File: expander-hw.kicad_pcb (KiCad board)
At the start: 2 copper layers, 44.2 x 22.6 mm, 29 parts, among them J1 Conn_ARM_SWD_TagConnect_TC203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, J2 USB_C_Receptacle_USB2.0_16P, J3 Conn_02x08_Odd_Even, U1 STM32H523RETx, U2 USBLC6-2SC6, U3 AZ1117-3.3, U4 SRDA3.3-4BTG, U5 SRDA3.3-4BTG, U6 SRDA3.3-4BTG

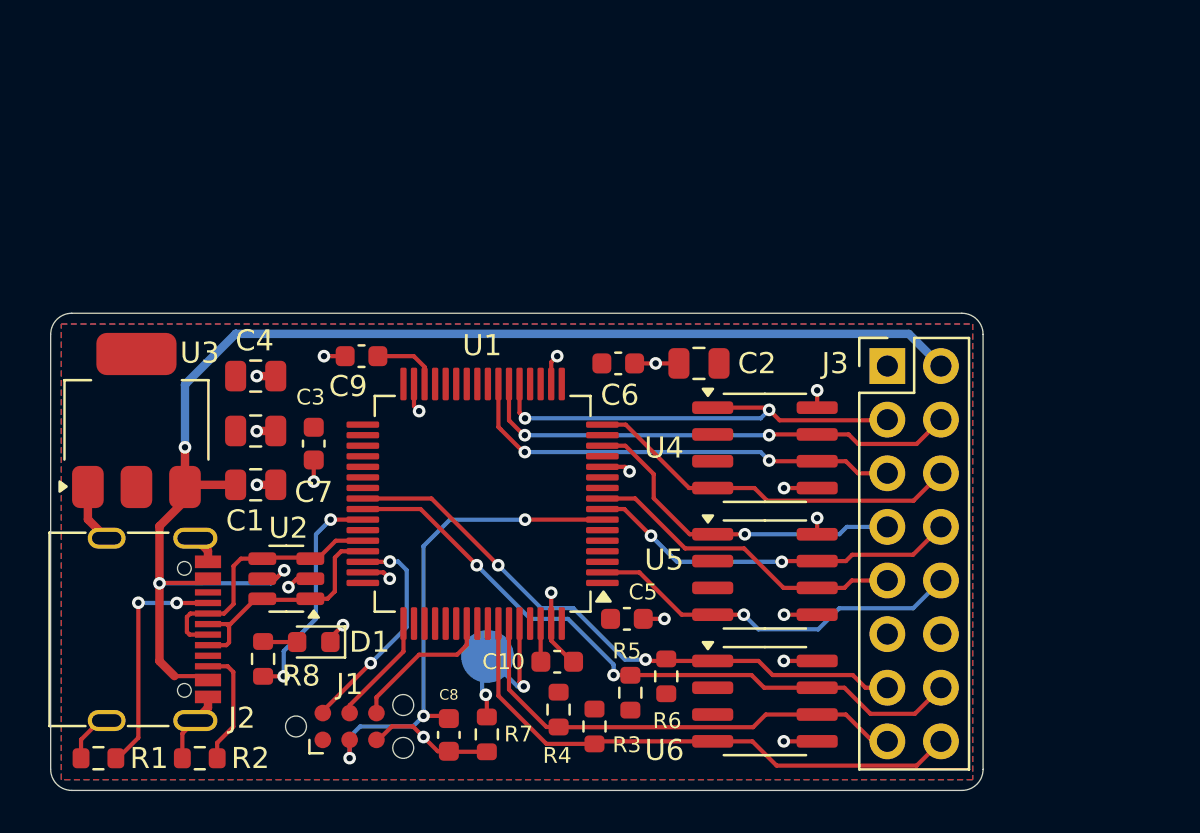
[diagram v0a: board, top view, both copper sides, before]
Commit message: Add DAC hardware
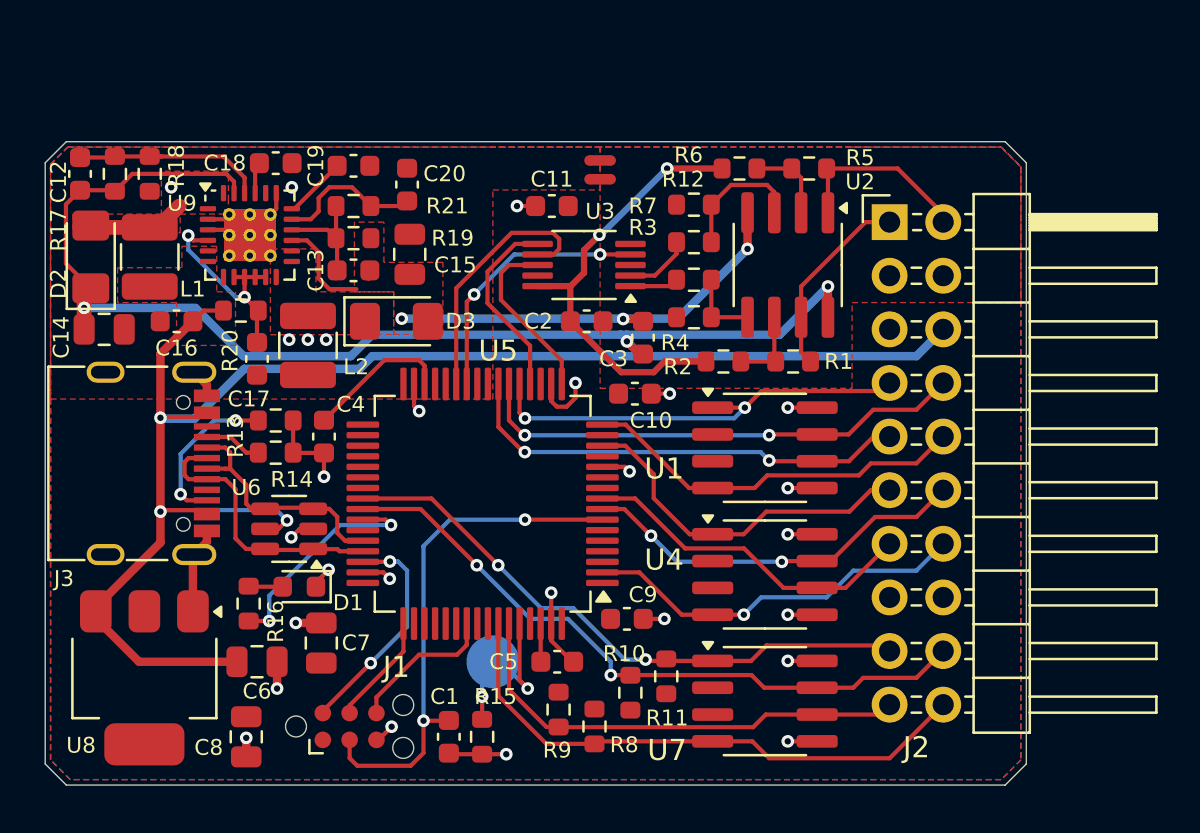
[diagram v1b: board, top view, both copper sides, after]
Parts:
- removed BOOT: TestPoint_Pad_D2.5mm, TestPoint:TestPoint_Pad_D2.5mm
- removed the J3 at (148.0, 92.9)
- added C12: 6.8pF, Capacitor_SMD:C_0603_1608Metric, F.Cu at (109.7, 83.8)
- added C13: 7.5pF, Capacitor_SMD:C_0603_1608Metric, F.Cu at (122.7, 88.4)
- added C14: 22uF, Capacitor_SMD:C_0805_2012Metric, F.Cu at (110.9, 91.2)
- added C15: 22uF, Capacitor_SMD:C_0805_2012Metric, F.Cu at (125.3, 87.6)
- added C16: 10uF, Capacitor_SMD:C_0603_1608Metric, F.Cu at (114.3, 90.8)
- added C17: 100nF, Capacitor_SMD:C_0603_1608Metric, F.Cu at (118.1, 92.6)
- added C18: 10nF, Capacitor_SMD:C_0603_1608Metric, F.Cu at (119.0, 83.3)
- added C19: 4.7nF, Capacitor_SMD:C_0603_1608Metric, F.Cu at (122.7, 83.4)
- added C20: 220nF, Capacitor_SMD:C_0603_1608Metric, F.Cu at (125.2, 84.3)
- added C3: 100nF, Capacitor_SMD:C_0603_1608Metric, F.Cu at (136.4, 91.6)
- added D2: D_Schottky, Diode_SMD:D_1206_3216Metric_Pad1.42x1.75mm_HandSolder, F.Cu at (110.2, 87.8)
- added D3: D_Schottky, Diode_SMD:D_1206_3216Metric_Pad1.42x1.75mm_HandSolder, F.Cu at (124.7, 90.8)
- added J2: Conn_02x10_Odd_Even, Connector_PinHeader_2.54mm:PinHeader_2x10_P2.54mm_Horizontal, F.Cu at (148.1, 86.1)
- added L1: 4.7uH, Inductor_SMD:L_1210_3225Metric, F.Cu at (113.0, 87.8)
- added L2: 4.7uH, Inductor_SMD:L_1210_3225Metric, F.Cu at (120.5, 91.9)
- added NT1: NetTie_2, NetTie:NetTie-2_SMD_Pad0.5mm, F.Cu at (134.4, 83.2)
- added NT2: NetTie_2, NetTie:NetTie-2_SMD_Pad0.5mm, F.Cu at (134.4, 84.1)
- added R1: 100k, Resistor_SMD:R_0603_1608Metric, F.Cu at (143.5, 92.7)
- added R12: 100k, Resistor_SMD:R_0603_1608Metric, F.Cu at (138.8, 85.3)
- added R17: 900k, Resistor_SMD:R_0603_1608Metric, F.Cu at (111.4, 83.8)
- added R18: 100k, Resistor_SMD:R_0603_1608Metric, F.Cu at (113.0, 83.8)
- added R19: 1M, Resistor_SMD:R_0603_1608Metric, F.Cu at (122.7, 86.9)
- added R2: 10k, Resistor_SMD:R_0603_1608Metric, F.Cu at (140.2, 92.7)
- added R20: 100, Resistor_SMD:R_0603_1608Metric, F.Cu at (117.3, 90.3)
- added R21: 100k, Resistor_SMD:R_0603_1608Metric, F.Cu at (122.7, 85.3)
- added R3: 10k, Resistor_SMD:R_0603_1608Metric, F.Cu at (138.8, 88.8)
- added R4: 100k, Resistor_SMD:R_0603_1608Metric, F.Cu at (138.8, 90.6)
- added R5: 100k, Resistor_SMD:R_0603_1608Metric, F.Cu at (144.3, 83.6)
- added R6: 10k, Resistor_SMD:R_0603_1608Metric, F.Cu at (141.0, 83.6)
- added R7: 10k, Resistor_SMD:R_0603_1608Metric, F.Cu at (138.8, 87.1)
- added TP1: BOOT, TestPoint:TestPoint_Pad_D2.5mm, B.Cu at (129.3, 106.9)
- added U2: OPA2994xD, Package_SO:SOIC-8_3.9x4.9mm_P1.27mm, F.Cu at (143.3, 88.1)
- added U3: DAC8562, Package_SO:VSSOP-10_3x3mm_P0.5mm, F.Cu at (133.6, 88.1)
- added U9: TPS65130RGE, Package_DFN_QFN:VQFN-24-1EP_4x4mm_P0.5mm_EP2.45x2.45mm_ThermalVias, F.Cu at (117.8, 86.7)
- C2: value 10uF -> 150nF; footprint Capacitor_SMD:C_0805_2012Metric -> Capacitor_SMD:C_0603_1608Metric
- moved C8 17.1 mm to (117.6, 110.5), turned to -90 degrees
- moved R14 16.7 mm to (119.0, 97.0), turned to 0 degrees
- moved R13 16.4 mm to (119.0, 95.5), turned to 0 degrees
- moved C11 15.9 mm to (132.1, 85.3), turned to 180 degrees
- moved U8 12.2 mm to (112.8, 107.7), turned to -90 degrees
- moved C7 10.5 mm to (121.2, 106.0), turned to 90 degrees
- moved C6 8.38 mm to (118.1, 106.9)
- moved J3 7.86 mm to (112.0, 97.5)
- moved C2 5.68 mm to (133.7, 90.8), turned to 0 degrees
- moved C4 4.20 mm to (121.3, 96.3), turned to -90 degrees
- moved R16 2.71 mm to (117.7, 104.2)
- moved D1 2.71 mm to (120.1, 103.4)
- moved U6 2.37 mm to (119.6, 100.6)
- moved C10 1.64 mm to (136.0, 94.2)
- moved R15 0.25 mm to (128.8, 110.5)
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- renumbered C8 to C1, C6 to C10, C7 to C11, C9 to C4, C10 to C5, C1 to C6, C3 to C7, C4 to C8, C5 to C9, J2 to J3, R5 to R10, R6 to R11, R2 to R13, R1 to R14, R7 to R15, R8 to R16, R3 to R8, R4 to R9, U4 to U1, U5 to U4, U1 to U5, U2 to U6, U6 to U7, U3 to U8
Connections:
- C2 pad 1: +3.3V -> Net-(U3-V_{REF}IN/OUT)
- C2 pad 2: GND -> GNDA
- U5 pad 17: unconnected-(U1-PA3-Pad17) -> /DAC_DIN
- U5 pad 20: unconnected-(U1-PA4-Pad20) -> /DAC_SYNC
- U5 pad 26: unconnected-(U1-PB0-Pad26) -> /DAC_LOAD
- U5 pad 27: unconnected-(U1-PB1-Pad27) -> /DAC_CLK
- U5 pad 33: /HW_V0 -> +3.3V
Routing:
- net +12V: track 0.00 -> 56.5 mm, vias 0 -> 3
- net -12V: track 0.00 -> 25.5 mm, vias 0 -> 3
- net Net-(U3-V_{REF}IN/OUT): track 0.00 -> 20.8 mm, vias 0 -> 2
- net /DAC_LOAD: track 0.00 -> 12.6 mm, vias 0 -> 2
- net /DAC_CLK: track 0.00 -> 12.2 mm
- net Net-(U9-ENN): track 0.00 -> 10.5 mm, vias 0 -> 2
- net VBUS: track 65.9 -> 75.5 mm
- net /A0: track 0.00 -> 9.19 mm
- net /DAC_SYNC: track 0.00 -> 9.08 mm
- net /A1: track 0.00 -> 8.92 mm
- net Net-(U9-FBP): track 0.00 -> 8.67 mm
- net /DAC_DIN: track 0.00 -> 8.34 mm
- net Net-(J3-CC1): track 11.2 -> 2.87 mm, vias 2 -> 0
- net Net-(U9-VREF): track 0.00 -> 6.96 mm
- net Net-(U2A-+): track 0.00 -> 6.27 mm
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- added copper zone on F.Cu, net -12V
- added copper zone on F.Cu, net CoilNeg
- added copper zone on F.Cu, net CoilPos
- added copper zone on F.Cu, net GND
- added copper zone on F.Cu, net GNDA
- added copper zone on F.Cu, net VBUS
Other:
- board size 44.2 x 22.6 mm -> 46.5 x 30.5 mm
- board text added: "HW-V1"
- board text removed: "HW-V0"

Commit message: Fix boost converter + vref
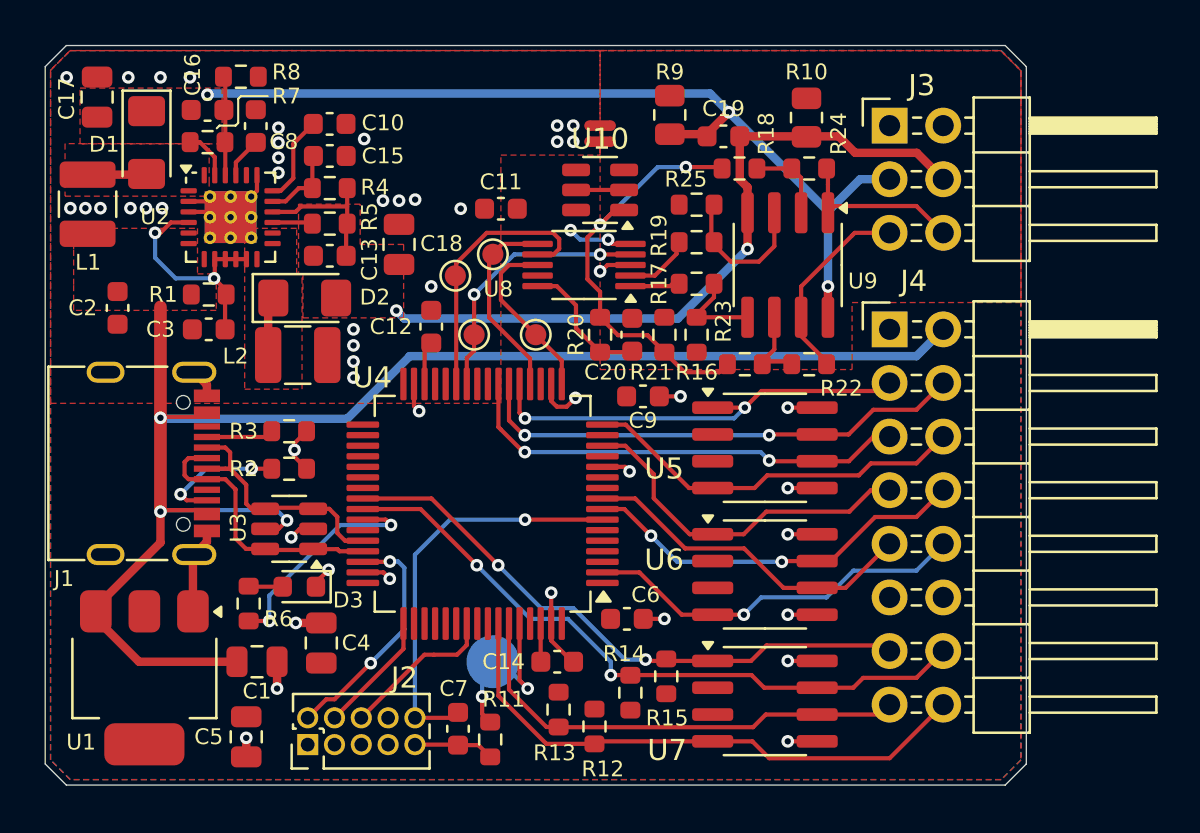
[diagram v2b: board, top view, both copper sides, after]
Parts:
- removed the J1 at (122.5, 110.0)
- added J3: Conn_02x03_Odd_Even, Connector_PinHeader_2.54mm:PinHeader_2x03_P2.54mm_Horizontal, F.Cu at (148.1, 81.5)
- added J4: Conn_02x08_Odd_Even, Connector_PinHeader_2.54mm:PinHeader_2x08_P2.54mm_Horizontal, F.Cu at (148.1, 91.2)
- added R10: 2k, Resistor_SMD:R_0805_2012Metric, F.Cu at (144.1, 81.2)
- added R20: 180, Resistor_SMD:R_0603_1608Metric, F.Cu at (134.4, 91.4)
- added R21: 180, Resistor_SMD:R_0603_1608Metric, F.Cu at (137.4, 91.4)
- added R9: 2k, Resistor_SMD:R_0805_2012Metric, F.Cu at (137.7, 81.0)
- added TP2: CLK, TestPoint:TestPoint_Pad_D1.0mm, F.Cu at (127.5, 88.6)
- added TP3: DIN, TestPoint:TestPoint_Pad_D1.0mm, F.Cu at (131.3, 91.4)
- added TP4: SYNC, TestPoint:TestPoint_Pad_D1.0mm, F.Cu at (129.3, 87.6)
- added TP5: LOAD, TestPoint:TestPoint_Pad_D1.0mm, F.Cu at (128.4, 91.4)
- added U10: MCP1501-10xCH, Package_TO_SOT_SMD:SOT-23-6, F.Cu at (134.4, 84.6)
- C20: renamed from C2; value 150nF -> 10nF
- J2: value Conn_02x10_Odd_Even -> Conn_ARM_JTAG_SWD_10; footprint Connector_PinHeader_2.54mm:PinHeader_2x10_P2.54mm_Horizontal -> Connector_PinHeader_1.27mm:PinHeader_2x05_P1.27mm_Vertical
- moved J2 37.1 mm to (120.5, 110.9), turned to 90 degrees
- moved C17 11.0 mm to (110.5, 80.2), turned to 90 degrees
- moved C19 10.3 mm to (140.2, 82.0), turned to 0 degrees
- moved C12 7.27 mm to (126.4, 91.1), turned to 90 degrees
- moved C16 6.76 mm to (115.8, 80.8), turned to 0 degrees
- moved R8 6.31 mm to (117.3, 79.2), turned to 180 degrees
- moved D1 6.03 mm to (112.9, 82.3), turned to -90 degrees
- moved R7 4.64 mm to (115.8, 82.3), turned to 180 degrees
- moved D2 4.48 mm to (120.4, 89.7)
- moved C15 3.91 mm to (121.6, 83.0), turned to 0 degrees
- moved L1 3.86 mm to (110.1, 85.3)
- moved C2 2.87 mm to (111.5, 90.2), turned to -90 degrees
- moved C3 2.68 mm to (115.8, 91.2), turned to 180 degrees
- moved C11 2.42 mm to (129.7, 85.5)
- moved R2 2.37 mm to (119.6, 97.8)
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- renumbered C6 to C1, C19 to C10, C4 to C12, C5 to C14, C20 to C15, C12 to C16, C14 to C17, C15 to C18, C3 to C19, C16 to C2, C17 to C3, C7 to C4, C8 to C5, C9 to C6, C1 to C7, C18 to C8, C10 to C9, D2 to D1, D3 to D2, D1 to D3, J3 to J1, R20 to R1, R15 to R11, R8 to R12, R9 to R13, R10 to R14, R11 to R15, R2 to R16, R3 to R17, R6 to R18, R7 to R19, R13 to R2, R1 to R22, R4 to R23, R5 to R24, R12 to R25, R14 to R3, R21 to R4, R19 to R5, R16 to R6, R17 to R7, R18 to R8, U8 to U1, U9 to U2, U6 to U3, U5 to U4, U1 to U5, U4 to U6, U3 to U8, U2 to U9
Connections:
- C13 pad 1: -12V -> Net-(U2-FBN)
- C13 pad 2: Net-(U9-FBN) -> -12V
- C15 pad 1: Net-(U9-VREF) -> Net-(U2-VREF)
- C20 pad 1: Net-(U3-V_{REF}IN/OUT) -> Net-(U8-V_{REF}IN/OUT)
- J2 pad 1: /A0 -> +3.3V
- J2 pad 10: /SPI1_CS -> /~{RESET}
- J2 pad 2: /A1 -> /SWDIO
- J2 pad 3: GNDA -> GND
- J2 pad 4: GNDA -> /SWDCLK
- J2 pad 5: +3.3V -> GND
- J2 pad 6: VBUS -> /SWO
- J2 pad 7: /SPI1_SCK -> unconnected-(J2-KEY-Pad7)
- J2 pad 8: /SPI1_MISO -> unconnected-(J2-NC/TDI-Pad8)
- J2 pad 9: /SPI1_MOSI -> GND
- R16 pad 2: Net-(U3-V_{REF}IN/OUT) -> Net-(U10-OUT)
- R18 pad 2: Net-(U3-V_{REF}IN/OUT) -> Net-(U10-OUT)
- R4 pad 1: Net-(U9-VREF) -> Net-(U2-FBN)
- R4 pad 2: Net-(U9-FBN) -> Net-(U2-VREF)
- R5 pad 1: Net-(U9-FBN) -> -12V
- R5 pad 2: -12V -> Net-(U2-FBN)
- U2 pad 16: Net-(U9-FBN) -> Net-(U2-FBN)
- U2 pad 17: Net-(U9-VREF) -> Net-(U2-VREF)
- U8 pad 10: Net-(U3-V_{REF}IN/OUT) -> Net-(U8-V_{REF}IN/OUT)
- U8 pad 3: GNDA -> GND
- U8 pad 5: /DAC_CLR -> +3.3V
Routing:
- net Net-(U3-V_{REF}IN/OUT): track 20.8 -> 0.00 mm, vias 2 -> 0
- net Net-(U10-OUT): track 0.00 -> 20.6 mm, vias 0 -> 2
- net -12V: track 25.5 -> 36.1 mm, vias 3 -> 2
- net +12V: track 56.5 -> 46.0 mm
- net Net-(U2-FBN): track 0.00 -> 6.99 mm
- net Net-(U9-VREF): track 6.96 -> 0.00 mm
- net Net-(U8-V_{REF}IN/OUT): track 0.00 -> 6.43 mm
- net /~{RESET}: track 24.9 -> 19.4 mm, vias 2 -> 1
- net Net-(U9-FBN): track 5.06 -> 0.00 mm
- net Net-(C12-Pad1): track 6.92 -> 2.07 mm
- net Net-(U2-FBP): track 8.67 -> 4.75 mm
- net Net-(U2-VREF): track 0.00 -> 3.72 mm
- net +3.3V: track 0.00 -> 3.10 mm, vias 0 -> 2
- net CoilNeg: track 0.00 -> 2.80 mm
- net GNDA: track 0.00 -> 2.28 mm
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- added copper zone on F.Cu, net +12V
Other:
- board size 46.5 x 30.5 mm -> 46.5 x 35 mm

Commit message: Refactor dac gain
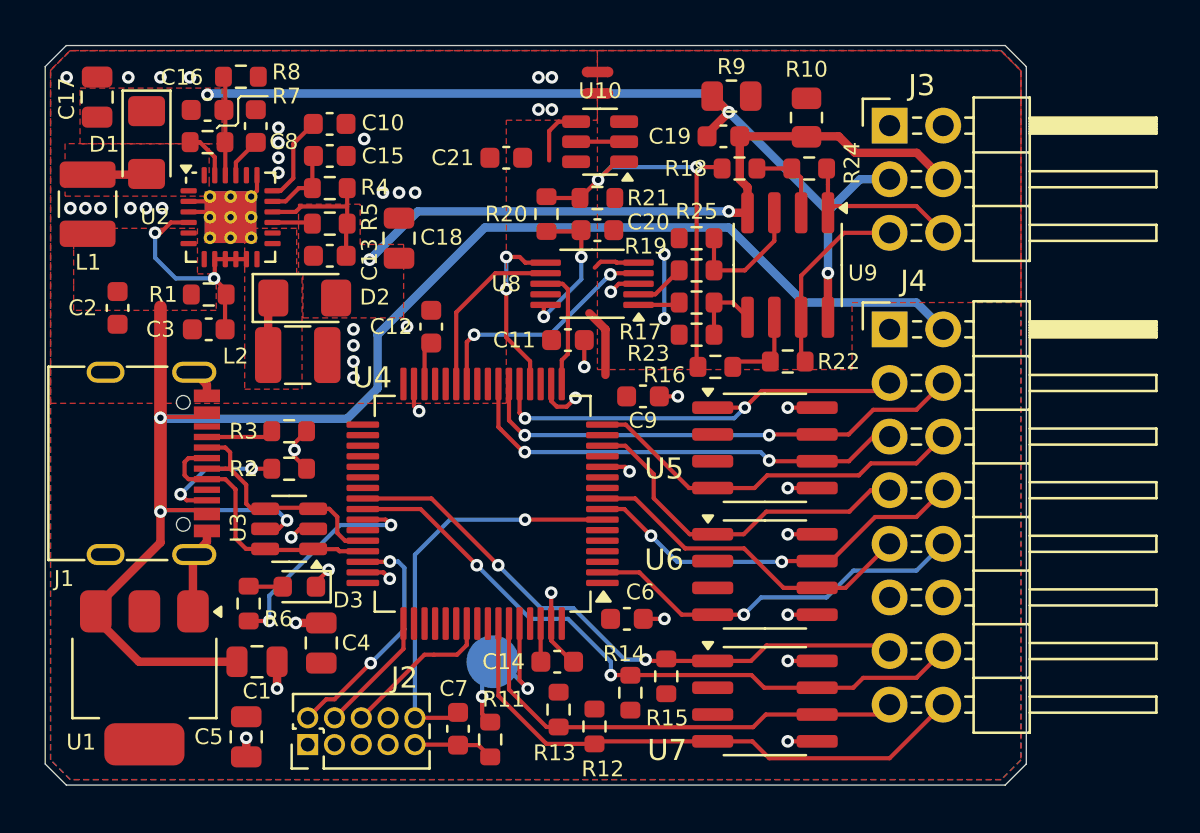
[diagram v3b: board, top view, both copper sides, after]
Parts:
- removed TP2: CLK, TestPoint:TestPoint_Pad_D1.0mm
- removed TP3: DIN, TestPoint:TestPoint_Pad_D1.0mm
- removed TP4: SYNC, TestPoint:TestPoint_Pad_D1.0mm
- removed TP5: LOAD, TestPoint:TestPoint_Pad_D1.0mm
- added C21: 100nF, Capacitor_SMD:C_0603_1608Metric, F.Cu at (129.9, 83.1)
- moved R21 7.21 mm to (134.2, 85.0), turned to 180 degrees
- moved C11 6.99 mm to (132.8, 91.7), turned to 0 degrees
- moved R20 6.25 mm to (131.8, 85.7)
- moved C20 5.22 mm to (134.2, 86.5), turned to 0 degrees
- moved R9 3.05 mm to (140.6, 80.1), turned to 180 degrees
- moved NT1 2.54 mm to (134.2, 79.0)
- moved NT2 2.29 mm to (134.2, 80.0)
- moved U10 2.29 mm to (134.4, 82.3)
- moved R25 1.59 mm to (138.9, 86.9)
- moved R16 1.40 mm to (139.8, 93.0)
- moved R19 1.33 mm to (138.9, 88.4)
- moved R22 1.02 mm to (143.3, 92.7)
- moved U8 0.97 mm to (134.0, 89.0)
- moved R17 0.89 mm to (138.9, 89.9)
- moved C18 0.29 mm to (124.8, 86.9)
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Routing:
- net VBUS: track 73.9 -> 79.4 mm
- net +3.3V: track 3.10 -> 8.30 mm, vias 2 -> 0
- net /DAC_CLK: track 12.9 -> 8.40 mm
- net GNDA: track 2.28 -> 5.33 mm, vias 0 -> 2
- net /DAC_DIN: track 8.34 -> 5.52 mm
- net /DAC_LOAD: track 12.6 -> 11.5 mm
- net Net-(U9B-+): track 4.64 -> 3.53 mm
- net -12V: track 36.1 -> 35.1 mm
- net Net-(U8-V_{REF}IN/OUT): track 6.43 -> 7.36 mm, vias 0 -> 2
- net /DAC_SYNC: track 9.37 -> 8.46 mm, vias 0 -> 2
- net GND: track 44.1 -> 44.8 mm
- net Net-(U8-V_{OUT}B): track 3.16 -> 2.40 mm
- net Net-(U9A-+): track 7.03 -> 6.29 mm
- net Net-(U9B--): track 3.73 -> 4.31 mm
- net +12V: track 46.0 -> 45.5 mm
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
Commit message: Small aesthetic changes
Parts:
- moved J3 0.51 mm to (148.1, 81.0)
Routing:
- net /SWDIO: track 11.3 -> 10.4 mm, vias 2 -> 1
- net /DAC_CLK: track 8.40 -> 7.65 mm
- net GND: track 44.8 -> 45.0 mm, vias 48 -> 47

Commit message: Minor refactoring
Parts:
- removed the C5 at (117.6, 110.5)
- C19: value 100nF -> 1uF
- C2: footprint Capacitor_SMD:C_0603_1608Metric -> Capacitor_SMD:C_0805_2012Metric
- C4: value 10uF -> 22uF
- D1, D2: footprint Diode_SMD:D_1206_3216Metric_Pad1.42x1.75mm_HandSolder -> Diode_SMD:D_1206_3216Metric
- R12, R13, R14, R15: value 5k1 -> 560
- R16, R17, R18, R19: value 10k -> 47k
- R22, R23, R24, R25: value 100k -> 470k
- R5: value 1M -> 1.1M
- R7: value 900k -> 1M
- moved C4 5.04 mm to (117.9, 109.9), turned to -90 degrees
- moved D2 0.23 mm to (120.1, 89.7)
- renumbered C21 to C11, C6 to C5, C9 to C6, C11 to C9
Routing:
- net GND: track 45.0 -> 43.5 mm, vias 47 -> 46
